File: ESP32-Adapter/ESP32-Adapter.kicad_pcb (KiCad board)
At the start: 2 copper layers, 80.1 x 88.5 mm, 24 parts, among them J10 Barrel_Jack, J12 Conn_01x05, J13 Conn_01x05, J5 Conn_01x03, U1 ICM-42670-P_Click, U2 LM317DCYR, U3 Adafruit CANPAL, U4 ADAFRUIT INA219 BREAKOUT, U5 ESP32-S3-DevKitC

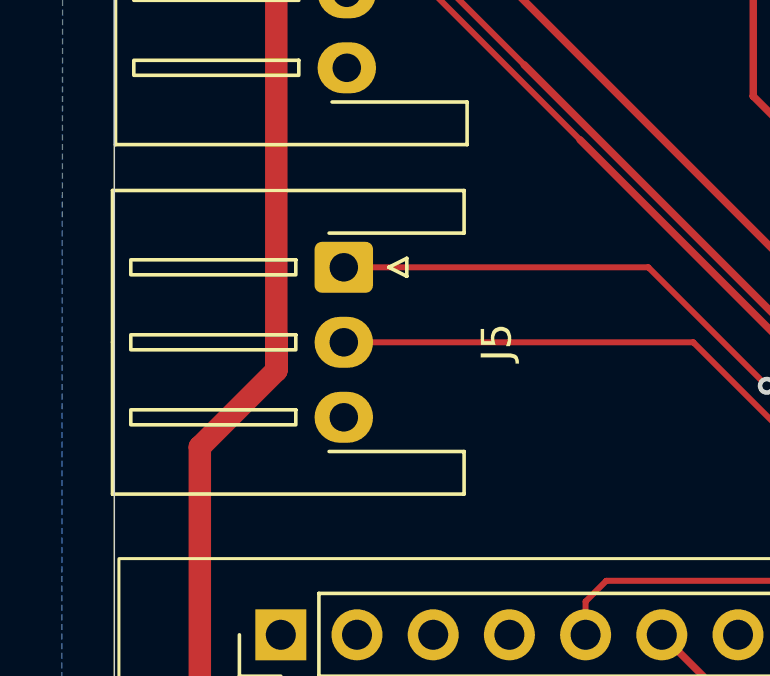
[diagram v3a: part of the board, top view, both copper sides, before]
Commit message: made j5 vertical as per jarad e
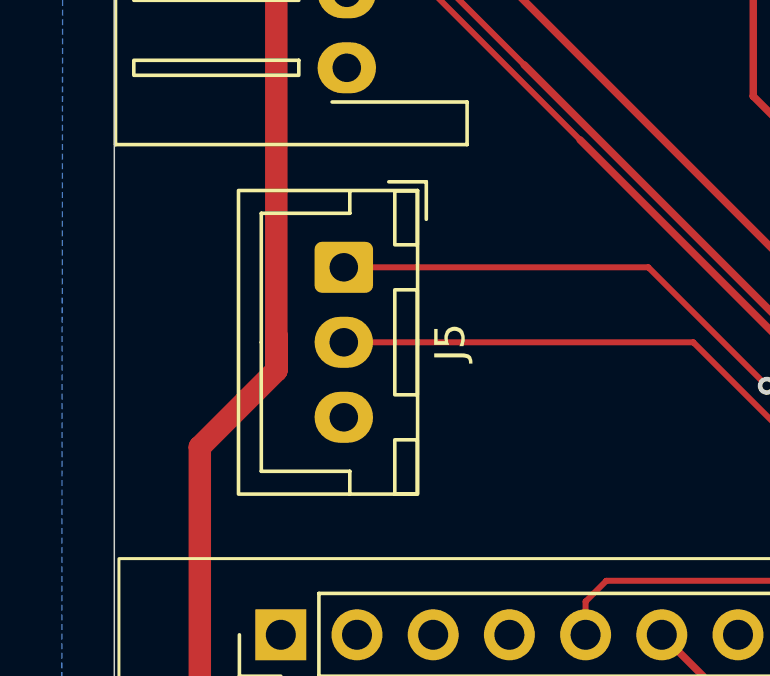
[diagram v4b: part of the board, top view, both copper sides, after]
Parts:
- J5: footprint Connector_JST:JST_XH_S3B-XH-A-1_1x03_P2.50mm_Horizontal -> Connector_JST:JST_XH_B3B-XH-A_1x03_P2.50mm_Vertical
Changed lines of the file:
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@@
 		)
 	)
-	(footprint "Connector_JST:JST_XH_S3B-XH-A-1_1x03_P2.50mm_Horizontal"
+	(footprint "Connector_JST:JST_XH_B3B-XH-A_1x03_P2.50mm_Vertical"
 		(layer "F.Cu")
 		(at 70.4709 72.55 -90)
-		(descr "JST XH series connector, S3B-XH-A-1 (http://www.jst-mfg.com/product/pdf/eng/eXH.pdf), generated with kicad-footprint-generator")
-		(tags "connector JST XH horizontal")
+		(descr "JST XH series connector, B3B-XH-A (http://www.jst-mfg.com/product/pdf/eng/eXH.pdf), generated with kicad-footprint-generator")
+		(tags "connector JST XH vertical")
 		(property "Reference" "J5"
-			(at 2.5 -5.1 90)
+			(at 2.5 -3.55 270)
 			(layer "F.SilkS")
 			(effects
@@
 		)
 		(property "Value" "Conn_01x03"
-			(at 2.5 8.8 90)
+			(at 2.5 4.6 270)
 			(layer "F.Fab")
 			(effects
@@
 		)
 		(property "Datasheet" "~"
-			(at 0 0 90)
+			(at 0 0 270)
 			(layer "F.Fab")
 			(hide yes)
@@
 		)
 		(property "Description" "Generic connector, single row, 01x03, script generated (kicad-library-utils/schlib/autogen/connector/)"
-			(at 0 0 90)
+			(at 0 0 270)
 			(layer "F.Fab")
 			(hide yes)
@@
 		(attr through_hole)
 		(fp_line
-			(start -2.56 7.71)
-			(end -2.56 -4.01)
-			(stroke
-				(width 0.12)
-				(type solid)
-			)
-			(layer "F.SilkS")
-		)
-		(fp_line
-			(start 2.5 7.71)
-			(end -2.56 7.71)
-			(stroke
-				(width 0.12)
-				(type solid)
-			)
-			(layer "F.SilkS")
-		)
-		(fp_line
-			(start 2.5 7.71)
-			(end 7.56 7.71)
-			(stroke
-				(width 0.12)
-				(type solid)
-			)
-			(layer "F.SilkS")
-		)
-		(fp_line
-			(start 7.56 7.71)
-			(end 7.56 -4.01)
-			(stroke
-				(width 0.12)
-				(type solid)
-			)
-			(layer "F.SilkS")
-		)
-		(fp_line
-			(start 0 -1.5)
-			(end -0.3 -2.1)
-			(stroke
-				(width 0.12)
-				(type solid)
-			)
-			(layer "F.SilkS")
-		)
-		(fp_line
-			(start -0.3 -2.1)
-			(end 0.3 -2.1)
-			(stroke
-				(width 0.12)
-				(type solid)
-			)
-			(layer "F.SilkS")
-		)
-		(fp_line
-			(start 0.3 -2.1)
-			(end 0 -1.5)
-			(stroke
-				(width 0.12)
-				(type solid)
-			)
-			(layer "F.SilkS")
-		)
-		(fp_line
-			(start -2.56 -4.01)
-			(end -1.14 -4.01)
-			(stroke
-				(width 0.12)
-				(type solid)
-			)
-			(layer "F.SilkS")
-		)
-		(fp_line
-			(start -1.14 -4.01)
-			(end -1.14 0.49)
-			(stroke
-				(width 0.12)
-				(type solid)
-			)
-			(layer "F.SilkS")
-		)
-		(fp_line
-			(start 6.14 -4.01)
-			(end 6.14 0.49)
-			(stroke
-				(width 0.12)
-				(type solid)
-			)
-			(layer "F.SilkS")
-		)
-		(fp_line
-			(start 7.56 -4.01)
-			(end 6.14 -4.01)
-			(stroke
-				(width 0.12)
-				(type solid)
-			)
-			(layer "F.SilkS")
-		)
-		(fp_rect
-			(start -0.25 1.6)
-			(end 0.25 7.1)
-			(stroke
-				(width 0.12)
-				(type solid)
-			)
-			(fill no)
-			(layer "F.SilkS")
-		)
-		(fp_rect
-			(start 2.25 1.6)
-			(end 2.75 7.1)
-			(stroke
-				(width 0.12)
-				(type solid)
-			)
-			(fill no)
-			(layer "F.SilkS")
-		)
-		(fp_rect
-			(start 4.75 1.6)
-			(end 5.25 7.1)
-			(stroke
-				(width 0.12)
-				(type solid)
-			)
-			(fill no)
-			(layer "F.SilkS")
-		)
-		(fp_rect
-			(start -2.95 -4.4)
-			(end 7.95 8.1)
+			(start -1.8 2.75)
+			(end 2.5 2.75)
+			(stroke
+				(width 0.12)
+				(type solid)
+			)
+			(layer "F.SilkS")
+		)
+		(fp_line
+			(start 6.8 2.75)
+			(end 2.5 2.75)
+			(stroke
+				(width 0.12)
+				(type solid)
+			)
+			(layer "F.SilkS")
+		)
+		(fp_line
+			(start -2.55 -0.2)
+			(end -1.8 -0.2)
+			(stroke
+				(width 0.12)
+				(type solid)
+			)
+			(layer "F.SilkS")
+		)
+		(fp_line
+			(start -1.8 -0.2)
+			(end -1.8 2.75)
+			(stroke
+				(width 0.12)
+				(type solid)
+			)
+			(layer "F.SilkS")
+		)
+		(fp_line
+			(start 6.8 -0.2)
+			(end 6.8 2.75)
+			(stroke
+				(width 0.12)
+				(type solid)
+			)
+			(layer "F.SilkS")
+		)
+		(fp_line
+			(start 7.55 -0.2)
+			(end 6.8 -0.2)
+			(stroke
+				(width 0.12)
+				(type solid)
+			)
+			(layer "F.SilkS")
+		)
+		(fp_line
+			(start -2.85 -2.75)
+			(end -2.85 -1.5)
+			(stroke
+				(width 0.12)
+				(type solid)
+			)
+			(layer "F.SilkS")
+		)
+		(fp_line
+			(start -1.6 -2.75)
+			(end -2.85 -2.75)
+			(stroke
+				(width 0.12)
+				(type solid)
+			)
+			(layer "F.SilkS")
+		)
+		(fp_rect
+			(start -2.55 -2.45)
+			(end -0.75 -1.7)
+			(stroke
+				(width 0.12)
+				(type solid)
+			)
+			(fill no)
+			(layer "F.SilkS")
+		)
+		(fp_rect
+			(start 0.75 -2.45)
+			(end 4.25 -1.7)
+			(stroke
+				(width 0.12)
+				(type solid)
+			)
+			(fill no)
+			(layer "F.SilkS")
+		)
+		(fp_rect
+			(start 5.75 -2.45)
+			(end 7.55 -1.7)
+			(stroke
+				(width 0.12)
+				(type solid)
+			)
+			(fill no)
+			(layer "F.SilkS")
+		)
+		(fp_rect
+			(start -2.56 -2.46)
+			(end 7.56 3.51)
+			(stroke
+				(width 0.12)
+				(type solid)
+			)
+			(fill no)
+			(layer "F.SilkS")
+		)
+		(fp_rect
+			(start -2.95 -2.85)
+			(end 7.95 3.9)
 			(stroke
 				(width 0.05)
@@
 		)
 		(fp_line
-			(start -2.45 7.6)
-			(end -2.45 -3.9)
+			(start 0 -1.35)
+			(end 0.625 -2.35)
 			(stroke
 				(width 0.1)
@@
 		)
 		(fp_line
-			(start 2.5 7.6)
-			(end -2.45 7.6)
+			(start -0.625 -2.35)
+			(end 0 -1.35)
 			(stroke
 				(width 0.1)
@@
 			(layer "F.Fab")
 		)
-		(fp_line
-			(start 2.5 7.6)
-			(end 7.45 7.6)
+		(fp_rect
+			(start -2.45 -2.35)
+			(end 7.45 3.4)
 			(stroke
 				(width 0.1)
 				(type solid)
 			)
-			(layer "F.Fab")
-		)
-		(fp_line
-			(start 7.45 7.6)
-			(end 7.45 -3.9)
-			(stroke
-				(width 0.1)
-				(type solid)
-			)
-			(layer "F.Fab")
-		)
-		(fp_line
-			(start -1.25 0.6)
-			(end 2.5 0.6)
-			(stroke
-				(width 0.1)
-				(type solid)
-			)
-			(layer "F.Fab")
-		)
-		(fp_line
-			(start -0.625 0.6)
-			(end 0 -0.4)
-			(stroke
-				(width 0.1)
-				(type solid)
-			)
-			(layer "F.Fab")
-		)
-		(fp_line
-			(start 6.25 0.6)
-			(end 2.5 0.6)
-			(stroke
-				(width 0.1)
-				(type solid)
-			)
-			(layer "F.Fab")
-		)
-		(fp_line
-			(start 0 -0.4)
-			(end 0.625 0.6)
-			(stroke
-				(width 0.1)
-				(type solid)
-			)
-			(layer "F.Fab")
-		)
-		(fp_line
-			(start -2.45 -3.9)
-			(end -1.25 -3.9)
-			(stroke
-				(width 0.1)
-				(type solid)
-			)
-			(layer "F.Fab")
-		)
-		(fp_line
-			(start -1.25 -3.9)
-			(end -1.25 0.6)
-			(stroke
-				(width 0.1)
-				(type solid)
-			)
-			(layer "F.Fab")
-		)
-		(fp_line
-			(start 6.25 -3.9)
-			(end 6.25 0.6)
-			(stroke
-				(width 0.1)
-				(type solid)
-			)
-			(layer "F.Fab")
-		)
-		(fp_line
-			(start 7.45 -3.9)
-			(end 6.25 -3.9)
-			(stroke
-				(width 0.1)
-				(type solid)
-			)
+			(fill no)
 			(layer "F.Fab")
 		)
 		(fp_text user "${REFERENCE}"
-			(at 2.5 1.85 90)
+			(at 2.5 2.7 270)
 			(layer "F.Fab")
 			(effects
@@
 		)
 		(embedded_fonts no)
-		(model "${KICAD9_3DMODEL_DIR}/Connector_JST.3dshapes/JST_XH_S3B-XH-A-1_1x03_P2.50mm_Horizontal.step"
+		(model "${KICAD9_3DMODEL_DIR}/Connector_JST.3dshapes/JST_XH_B3B-XH-A_1x03_P2.50mm_Vertical.step"
 			(offset
 				(xyz 0 0 0)
